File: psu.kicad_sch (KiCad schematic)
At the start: 1 part, among them J13 Conn_02x02_Odd_Even

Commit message: sch, pcb: update pn fields
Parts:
- J13: Part Number (none) -> 0430450400
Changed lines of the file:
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@@
+			)
+		)
+		(property "Part Number" "0430450400"
+			(at 95.25 100.33 0)
+			(effects
+				(font
+					(size 1.27 1.27)
+				)
+				(hide yes)
 			)
 		)

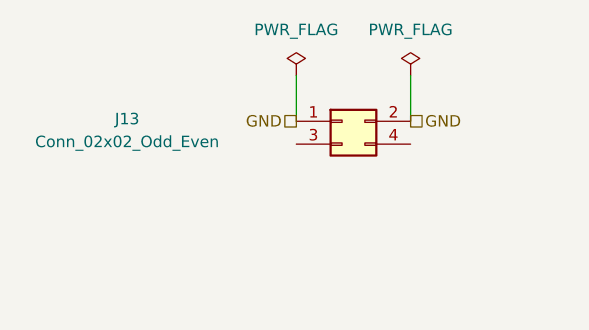
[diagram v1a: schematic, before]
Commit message: docs: add ibom, pcb, psu: fuse, pgmmux, pcb: 2.00mm headers -> 2.54
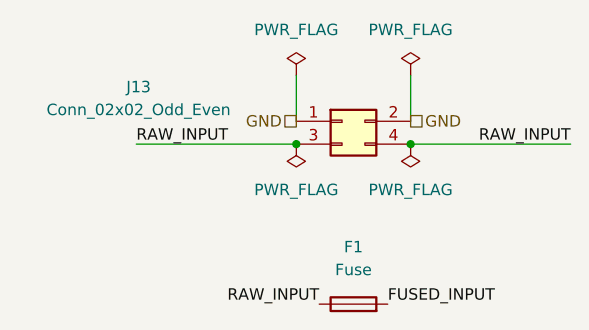
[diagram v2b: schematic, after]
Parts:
- added F1: Fuse, Fuse:Fuseholder_Blade_Mini_Keystone_3568, symbol Device:Fuse
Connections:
- net RAW_INPUT: now reaches J13.3 (Pin_3)
- net RAW_INPUT: now also J13.4 (Pin_4), F1.1
- new net FUSED_INPUT: F1.2

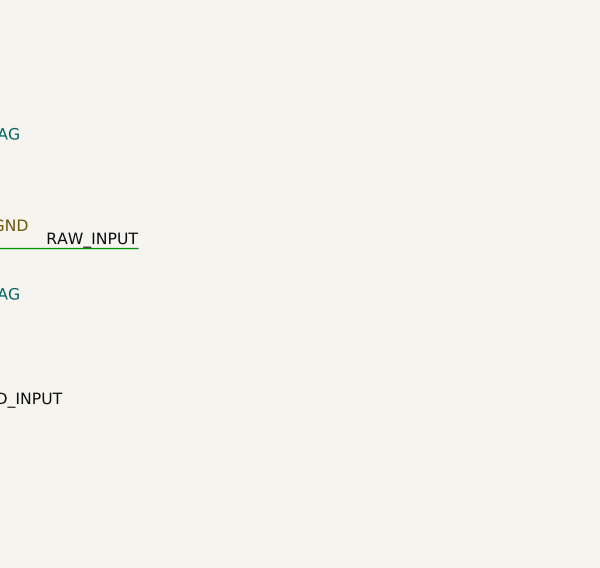
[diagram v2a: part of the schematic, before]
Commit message: sym: TMUX1511, psu: add failsafe development
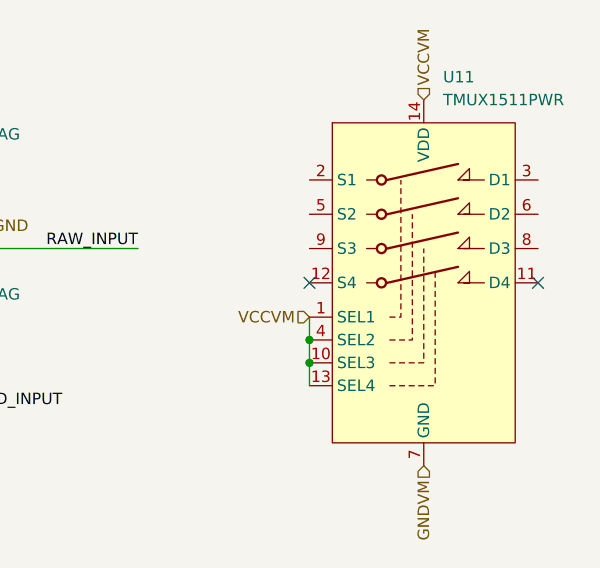
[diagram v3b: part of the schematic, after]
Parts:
- added U11: TMUX1511PWR, Package_SO:TSSOP-14_4.4x5mm_P0.65mm, symbol Analog_Switch_Local:TMUX1511PWR
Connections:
- new net GNDVM: U11.7 (GND)
- new net VCCVM: U11.1 (SEL1), U11.10 (SEL3), U11.13 (SEL4), U11.14 (VDD), U11.4 (SEL2)
- no-connect marks 0 -> 2
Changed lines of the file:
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@@
+	)
+	(junction
+		(at 139.7 113.03)
+		(diameter 0)
+		(color 0 0 0 0)
 	)
 	(junction
@@
 		(color 0 0 0 0)
 	)
+	(junction
+		(at 139.7 115.57)
+		(diameter 0)
+		(color 0 0 0 0)
+	)
+	(no_connect
+		(at 165.1 106.68)
+	)
+	(no_connect
+		(at 139.7 106.68)
+	)
 	(wire
 		(pts
@@
 		(pts
 			(xy 120.65 102.87) (xy 102.87 102.87)
+		)
+		(stroke
+			(width 0)
+			(type default)
+		)
+	)
+	(wire
+		(pts
+			(xy 139.7 110.49) (xy 139.7 113.03)
+		)
+		(stroke
+			(width 0)
+			(type default)
+		)
+	)
+	(wire
+		(pts
+			(xy 139.7 115.57) (xy 139.7 118.11)
+		)
+		(stroke
+			(width 0)
+			(type default)
+		)
+	)
+	(wire
+		(pts
+			(xy 139.7 113.03) (xy 139.7 115.57)
 		)
 		(stroke
@@
 			)
 			(justify left bottom)
+		)
+	)
+	(hierarchical_label "GNDVM"
+		(shape input)
+		(at 152.4 127 270)
+		(effects
+			(font
+				(size 1.27 1.27)
+			)
+			(justify right)
+		)
+	)
+	(hierarchical_label "VCCVM"
+		(shape input)
+		(at 152.4 86.36 90)
+		(effects
+			(font
+				(size 1.27 1.27)
+			)
+			(justify left)
 		)
 	)
@@
 		)
 	)
+	(hierarchical_label "VCCVM"
+		(shape input)
+		(at 139.7 110.49 180)
+		(effects
+			(font
+				(size 1.27 1.27)
+			)
+			(justify right)
+		)
+	)
 	(hierarchical_label "GND"
 		(shape passive)
@@
 		)
 	)
+	(symbol
+		(lib_id "Analog_Switch_Local:TMUX1511PWR")
+		(at 152.4 106.68 0)
+		(unit 1)
+		(exclude_from_sim no)
+		(in_bom yes)
+		(on_board yes)
+		(dnp no)
+		(fields_autoplaced yes)
+		(property "Reference" "U11"
+			(at 154.5433 83.82 0)
+			(effects
+				(font
+					(size 1.27 1.27)
+				)
+				(justify left)
+			)
+		)
+		(property "Value" "TMUX1511PWR"
+			(at 154.5433 86.36 0)
+			(effects
+				(font
+					(size 1.27 1.27)
+				)
+				(justify left)
+			)
+		)
+		(property "Footprint" "Package_SO:TSSOP-14_4.4x5mm_P0.65mm"
+			(at 172.72 123.19 0)
+			(effects
+				(font
+					(size 1.27 1.27)
+				)
+				(hide yes)
+			)
+		)
+		(property "Datasheet" "https://www.ti.com/lit/ds/symlink/tmux1511.pdf?ts=1744449756224&ref_url=https%253A%252F%252Fwww.ti.com%252Fproduct%252FTMUX1511"
+			(at 177.8 125.73 0)
+			(effects
+				(font
+					(size 1.27 1.27)
+				)
+				(hide yes)
+			)
+		)
+		(property "Description" "Low-Capacitance, 1:1 (SPST) 4-Channel, Powered-Off Protected Switch with 1.8V Logic"
+			(at 152.4 71.628 0)
+			(effects
+				(font
+					(size 1.27 1.27)
+				)
+				(hide yes)
+			)
+		)
+		(pin "1"
+		)
+		(pin "9"
+		)
+		(pin "5"
+		)
+		(pin "2"
+		)
+		(pin "6"
+		)
+		(pin "7"
+		)
+		(pin "14"
+		)
+		(pin "11"
+		)
+		(pin "13"
+		)
+		(pin "3"
+		)
+		(pin "10"
+		)
+		(pin "4"
+		)
+		(pin "12"
+		)
+		(pin "8"
+		)
+		(instances
+			(project ""
+				(path "/362ca48c-0b77-4943-b8b3-fc15ab97f30d/083e4746-c54f-4ebf-8db7-bc4666178b1b"
+					(reference "U11")
+					(unit 1)
+				)
+			)
+		)
+	)

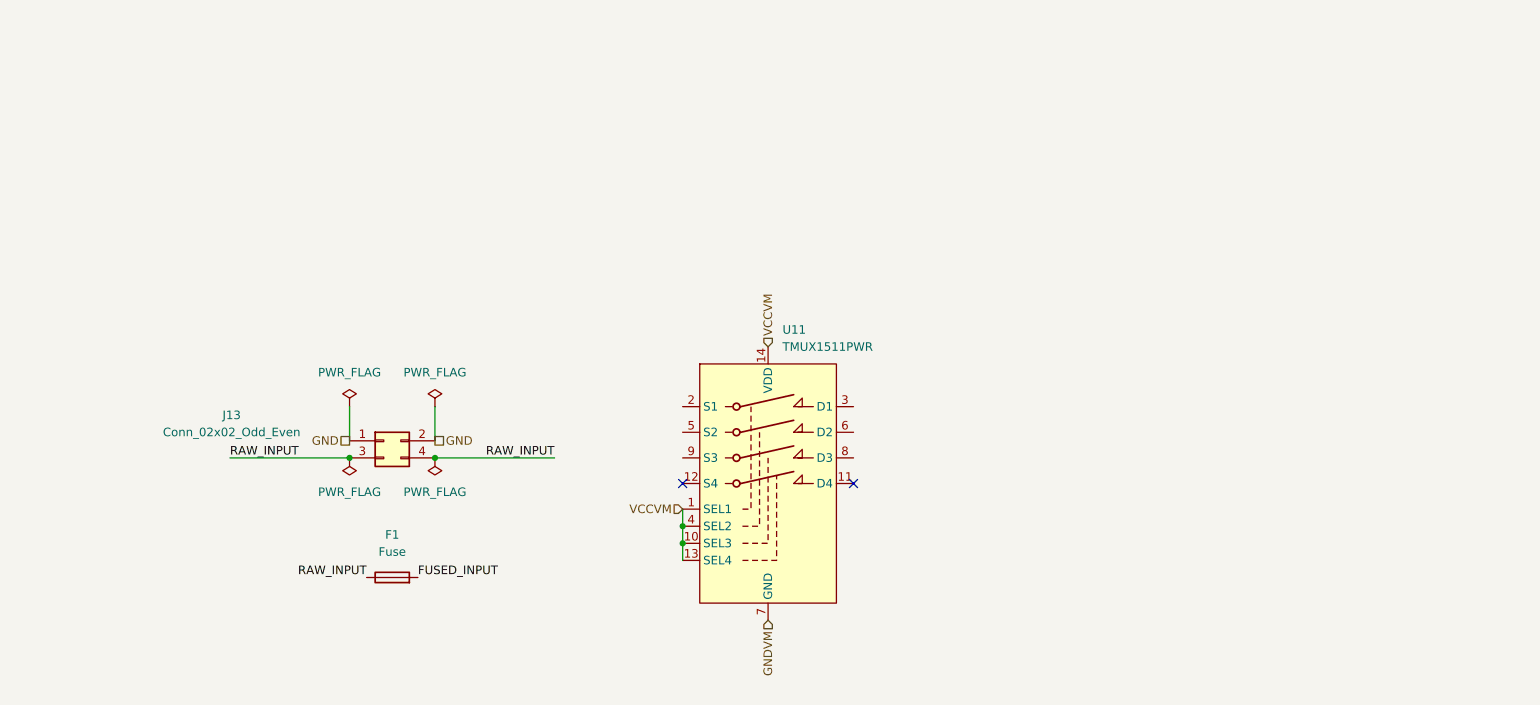
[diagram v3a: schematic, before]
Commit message: psu, sch, pcb: voltmeters
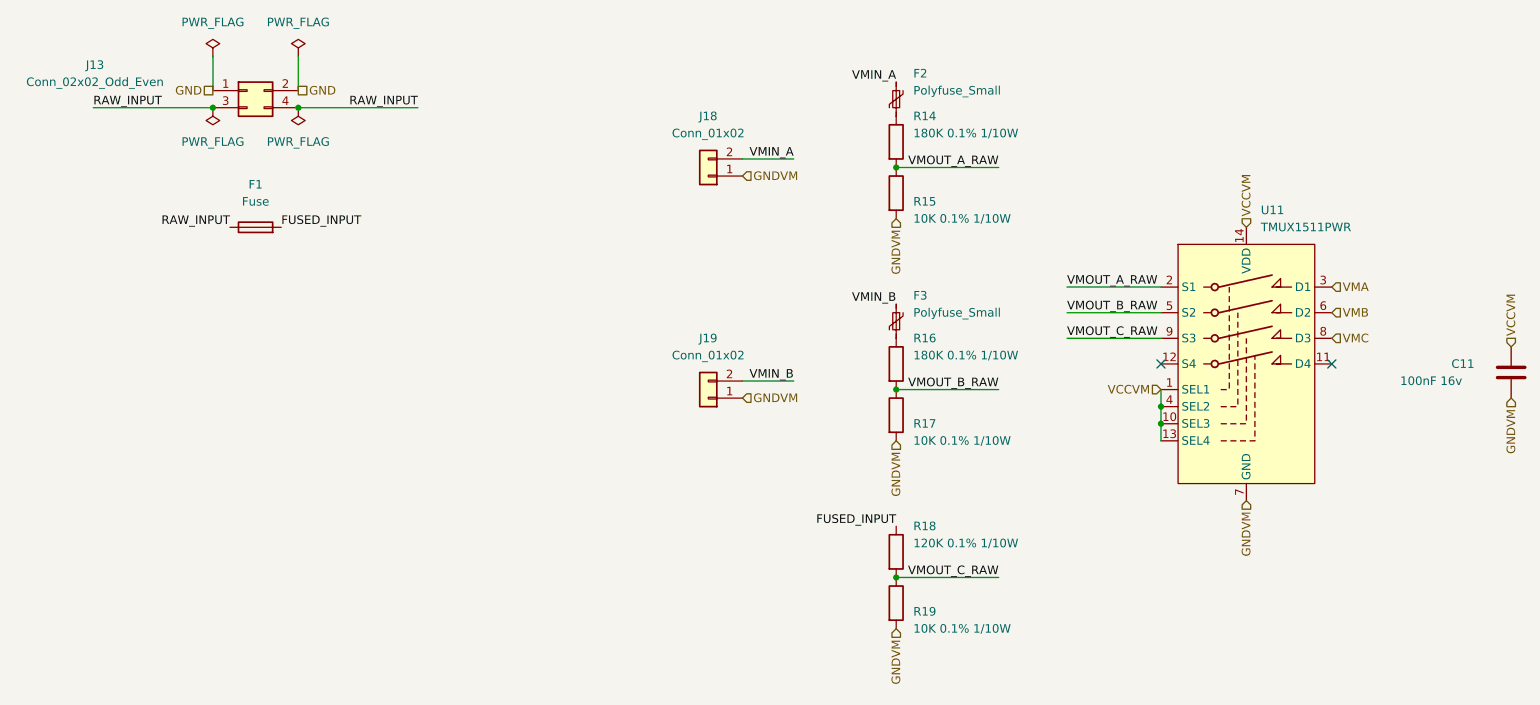
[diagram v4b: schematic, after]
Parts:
- added C11: 100nF 16v, Capacitor_SMD:C_0402_1005Metric, symbol Device:C
- added F2, F3: Polyfuse_Small, Fuse:Fuse_1206_3216Metric_Pad1.42x1.75mm_HandSolder, symbol Device:Polyfuse_Small
- added J18, J19: Conn_01x02, Connector_Molex:Molex_Nano-Fit_105313-xx02_1x02_P2.50mm_Horizontal, symbol Connector_Generic:Conn_01x02
- added R14, R16: 180K 0.1% 1/10W, Resistor_SMD:R_0603_1608Metric, symbol Device:R
- added R15, R17, R19: 10K 0.1% 1/10W, Resistor_SMD:R_0603_1608Metric, symbol Device:R
- added R18: 120K 0.1% 1/10W, Resistor_SMD:R_0603_1608Metric, symbol Device:R
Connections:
- net FUSED_INPUT: now also R18.1
- net GNDVM: now also C11.1, J18.1 (Pin_1), J19.1 (Pin_1), R15.2, R17.2, R19.2
- net VCCVM: now also C11.2
- net VMOUT_A_RAW: now reaches U11.2 (S1)
- net VMOUT_A_RAW: now also R14.2, R15.1
- net VMA: now reaches U11.3 (D1)
- net VMOUT_B_RAW: now reaches U11.5 (S2)
- net VMOUT_B_RAW: now also R16.2, R17.1
- net VMB: now reaches U11.6 (D2)
- net VMC: now reaches U11.8 (D3)
- net VMOUT_C_RAW: now reaches U11.9 (S3)
- net VMOUT_C_RAW: now also R18.2, R19.1
- new net: F3.2, R16.1
- new net: F2.2, R14.1
- new net VMIN_A: F2.1, J18.2 (Pin_2)
- new net VMIN_B: F3.1, J19.2 (Pin_2)
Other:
- moved on the sheet: F1, J13, U11

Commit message: sch, pcb: add part numbers
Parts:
- J18, J19: Part Number (none) -> 1053132102
- U11: Part Number (none) -> TMUX1511PWR
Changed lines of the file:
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@@
+			)
+		)
+		(property "Part Number" "TMUX1511PWR"
+			(at 223.52 88.9 0)
+			(effects
+				(font
+					(size 1.27 1.27)
+				)
+				(hide yes)
 			)
 		)
@@
 			)
 		)
+		(property "Part Number" "1053132102"
+			(at 143.51 93.98 0)
+			(effects
+				(font
+					(size 1.27 1.27)
+				)
+				(hide yes)
+			)
+		)
 		(pin "2"
 		)
@@
 			(at 143.51 60.96 0)
 			(effects
+				(font
+					(size 1.27 1.27)
+				)
+				(hide yes)
+			)
+		)
+		(property "Part Number" "1053132102"
+			(at 143.51 60.96 0)
+			(effects

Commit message: psu, pcb: 5v pwr led
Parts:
- added D5: LED, LED_SMD:LED_0603_1608Metric, symbol Device:LED
- added R20: 330R, Resistor_SMD:R_0603_1608Metric, symbol Device:R
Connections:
- net GND: now also D5.1 (K)
- new net: D5.2 (A), R20.1
- new net +5V: R20.2

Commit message: buck, pcb, misc: add buck psu
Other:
- added sheet PSU (buck.kicad_sch)
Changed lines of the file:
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@@
+		)
+	)
+	(label "FUSED_INPUT"
+		(at 55.88 80.01 180)
+		(effects
+			(font
+				(size 1.27 1.27)
+			)
+			(justify right bottom)
 		)
 	)
@@
 	)
 	(symbol
+		(lib_id "power:+5V")
+		(at 93.98 80.01 270)
+		(unit 1)
+		(exclude_from_sim no)
+		(in_bom yes)
+		(on_board yes)
+		(dnp no)
+		(fields_autoplaced yes)
+		(property "Reference" "#PWR060"
+			(at 90.17 80.01 0)
+			(effects
+				(font
+					(size 1.27 1.27)
+				)
+				(hide yes)
+			)
+		)
+		(property "Value" "+5V"
+			(at 97.79 80.0099 90)
+			(effects
+				(font
+					(size 1.27 1.27)
+				)
+				(justify left)
+			)
+		)
+		(property "Footprint" ""
+			(at 93.98 80.01 0)
+			(effects
+				(font
+					(size 1.27 1.27)
+				)
+				(hide yes)
+			)
+		)
+		(property "Datasheet" ""
+			(at 93.98 80.01 0)
+			(effects
+				(font
+					(size 1.27 1.27)
+				)
+				(hide yes)
+			)
+		)
+		(property "Description" "Power symbol creates a global label with name \"+5V\""
+			(at 93.98 80.01 0)
+			(effects
+				(font
+					(size 1.27 1.27)
+				)
+				(hide yes)
+			)
+		)
+		(pin "1"
+		)
+		(instances
+			(project "P2 Kevinbot Board"
+				(path "/362ca48c-0b77-4943-b8b3-fc15ab97f30d/083e4746-c54f-4ebf-8db7-bc4666178b1b"
+					(reference "#PWR060")
+					(unit 1)
+				)
+			)
+		)
+	)
+	(symbol
 		(lib_id "Device:Polyfuse_Small")
 		(at 171.45 82.55 0)
@@
 				)
 			)
+		)
+	)
+	(sheet
+		(at 55.88 76.2)
+		(size 38.1 7.62)
+		(exclude_from_sim no)
+		(in_bom yes)
+		(on_board yes)
+		(dnp no)
+		(fields_autoplaced yes)
+		(stroke
+			(width 0.1524)
+			(type solid)
+		)
+		(fill
+			(color 0 0 0 0.0000)
+		)
+		(property "Sheetname" "PSU"
+			(at 55.88 75.4884 0)
+			(effects
+				(font
+					(size 1.27 1.27)
+				)
+				(justify left bottom)
+			)
+		)
+		(property "Sheetfile" "buck.kicad_sch"
+			(at 55.88 84.4046 0)
+			(effects
+				(font
+					(size 1.27 1.27)
+				)
+				(justify left top)
+			)
+		)
+		(pin "5VOUT" output
+			(at 93.98 80.01 0)
+			(effects
+				(font
+					(size 1.27 1.27)
+				)
+				(justify right)
+			)
+		)
+		(pin "VIN" input
+			(at 55.88 80.01 180)
+			(effects
+				(font
+					(size 1.27 1.27)
+				)
+				(justify left)
+			)
+		)
+		(instances
+			(project "P2 Kevinbot Board"
+				(path "/362ca48c-0b77-4943-b8b3-fc15ab97f30d/083e4746-c54f-4ebf-8db7-bc4666178b1b"
+					(page "11")
+				)
+			)

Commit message: sch: erc
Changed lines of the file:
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@@
 	(paper "A4")
-	(junction
-		(at 82.55 50.8)
-		(diameter 0)
-		(color 0 0 0 0)
-	)
 	(junction
 		(at 210.82 95.25)
@@
 	(no_connect
 		(at 210.82 88.9)
-	)
-	(wire
-		(pts
-			(xy 82.55 43.18) (xy 82.55 48.26)
-		)
-		(stroke
-			(width 0)
-			(type default)
-		)
 	)
 	(wire
@@
 	)
 	(symbol
-		(lib_id "power:PWR_FLAG")
-		(at 82.55 50.8 180)
-		(unit 1)
-		(exclude_from_sim no)
-		(in_bom yes)
-		(on_board yes)
-		(dnp no)
-		(fields_autoplaced yes)
-		(property "Reference" "#FLG03"
-			(at 82.55 52.705 0)
-			(effects
-				(font
-					(size 1.27 1.27)
-				)
-				(hide yes)
-			)
-		)
-		(property "Value" "PWR_FLAG"
-			(at 82.55 55.88 0)
-			(effects
-				(font
-					(size 1.27 1.27)
-				)
-			)
-		)
-		(property "Footprint" ""
-			(at 82.55 50.8 0)
-			(effects
-				(font
-					(size 1.27 1.27)
-				)
-				(hide yes)
-			)
-		)
-		(property "Datasheet" "~"
-			(at 82.55 50.8 0)
-			(effects
-				(font
-					(size 1.27 1.27)
-				)
-				(hide yes)
-			)
-		)
-		(property "Description" "Special symbol for telling ERC where power comes from"
-			(at 82.55 50.8 0)
-			(effects
-				(font
-					(size 1.27 1.27)
-				)
-				(hide yes)
-			)
-		)
-		(pin "1"
-		)
-		(instances
-			(project ""
-				(path "/362ca48c-0b77-4943-b8b3-fc15ab97f30d/083e4746-c54f-4ebf-8db7-bc4666178b1b"
-					(reference "#FLG03")
-					(unit 1)
-				)
-			)
-		)
-	)
-	(symbol
 		(lib_id "Device:R")
 		(at 171.45 116.84 0)
@@
 	)
 	(symbol
-		(lib_id "power:PWR_FLAG")
-		(at 82.55 43.18 0)
-		(unit 1)
-		(exclude_from_sim no)
-		(in_bom yes)
-		(on_board yes)
-		(dnp no)
-		(fields_autoplaced yes)
-		(property "Reference" "#FLG02"
-			(at 82.55 41.275 0)
-			(effects
-				(font
-					(size 1.27 1.27)
-				)
-				(hide yes)
-			)
-		)
-		(property "Value" "PWR_FLAG"
-			(at 82.55 38.1 0)
-			(effects
-				(font
-					(size 1.27 1.27)
-				)
-			)
-		)
-		(property "Footprint" ""
-			(at 82.55 43.18 0)
-			(effects
-				(font
-					(size 1.27 1.27)
-				)
-				(hide yes)
-			)
-		)
-		(property "Datasheet" "~"
-			(at 82.55 43.18 0)
-			(effects
-				(font
-					(size 1.27 1.27)
-				)
-				(hide yes)
-			)
-		)
-		(property "Description" "Special symbol for telling ERC where power comes from"
-			(at 82.55 43.18 0)
-			(effects
-				(font
-					(size 1.27 1.27)
-				)
-				(hide yes)
-			)
-		)
-		(pin "1"
-		)
-		(instances
-			(project "P2 Kevinbot Board"
-				(path "/362ca48c-0b77-4943-b8b3-fc15ab97f30d/083e4746-c54f-4ebf-8db7-bc4666178b1b"
-					(reference "#FLG02")
-					(unit 1)
-				)
-			)
-		)
-	)
-	(symbol
 		(lib_id "Connector_Generic:Conn_02x02_Odd_Even")
 		(at 74.93 48.26 0)
@@
 			)
 		)
-		(property "Datasheet" "https://www.we-online.com/katalog/datasheet/150080SS75000.pdf"
+		(property "Datasheet" "~"
 			(at 71.12 100.33 0)
 			(effects
@@
 			)
 		)
-		(property "Sim.Pins" "1=A 2=K"
+		(property "Sim.Pins" "1=K 2=A"
 			(at 71.12 100.33 0)
 			(effects
